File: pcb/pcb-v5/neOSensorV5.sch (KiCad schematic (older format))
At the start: 14 parts

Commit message: update pcb v5
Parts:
- removed J?: Conn_01x04, symbol Connector_Generic:Conn_01x04
- removed J?: Conn_01x08, symbol Connector_Generic:Conn_01x08
- added C?: 100nF, Resistor_SMD:R_0805_2012Metric_Pad1.20x1.40mm_HandSolder, symbol Device:C_Small
- added J?: Conn_01x05, Connector_PinHeader_2.54mm:PinHeader_1x05_P2.54mm_Vertical, symbol Connector_Generic:Conn_01x05
- added R? (x2): 4K7, symbol Device:R_Small
- added TP?: tp_tx2, TestPoint:TestPoint_Loop_D2.50mm_Drill1.0mm, symbol Connector:TestPoint
- added TP?: tp_rx2, TestPoint:TestPoint_Loop_D2.50mm_Drill1.0mm, symbol Connector:TestPoint
- C?: footprint (none) -> Capacitor_THT:CP_Radial_D6.3mm_P2.50mm
- H? (x2): value MountingHole_Pad -> 3.2mm for MH3 screw; footprint (none) -> MountingHole:MountingHole_3.2mm_M3_Pad
- J? (x2): footprint (none) -> Connector_PinHeader_2.54mm:PinHeader_1x04_P2.54mm_Vertical
- J? (x2): footprint (none) -> Connector_PinHeader_2.54mm:PinHeader_1x05_P2.54mm_Vertical
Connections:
- net labels added: +3V3, LED, PM_EN, RX2, TX2
- net labels removed: VIN
- wire segments 42 -> 68
- no-connect marks 0 -> 3
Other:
- note added: "Display"
- note added: "Notes about Particule Meters sensors\n- PM_EN is optionnally intended to enable/disable the\nparticule meter (not to have it always on)"
- note added: "Notes:\n- GPIO13 reserved for noise sensor\n- GPIO5 reserved for LED + clear sw\n- GPIO4 reserved for IR sensor (really?)\n- GPIO1 & GPIO3 are serial0 (prog.)\n- +3V3 on EN pin is optional"
- note added: "Power supply"
- note added: "TODO:\n- associate INT with an ESP32 pin"
- moved on the sheet: C?, H?, U?

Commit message: update
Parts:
- added D1: Red, LED_SMD:LED_0805_2012Metric_Pad1.15x1.40mm_HandSolder, symbol Device:LED_Small_ALT
- added Q1: 2N7002, Package_TO_SOT_SMD:SOT-23, symbol Transistor_FET:2N7002
- added R1: 68, Resistor_SMD:R_0805_2012Metric_Pad1.20x1.40mm_HandSolder, symbol Device:R_Small
- added R2, R9: 15k, Resistor_SMD:R_0805_2012Metric_Pad1.20x1.40mm_HandSolder, symbol Device:R_Small
- added R3, R7: 470, Resistor_SMD:R_0805_2012Metric_Pad1.20x1.40mm_HandSolder, symbol Device:R_Small
- added SW1: clear, neosensor_addon:G71Y_µsw_smd, symbol neosensor_addon:G71Y
- added U1: HC-SR01, neosensor_addon:PIR_HC-SR01, symbol neosensor_addon:HC-SR01
- R4, R8: renamed from R?; footprint (none) -> Resistor_SMD:R_0805_2012Metric_Pad1.20x1.40mm_HandSolder
- R5, R6: renamed from R?; value 220 -> 470; footprint (none) -> Resistor_SMD:R_0805_2012Metric_Pad1.20x1.40mm_HandSolder
- gave numbers to parts that had none: 14
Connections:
- net +3V3: now also SW1.2
- net +5V: now also D1.2 (A), U1.1 (V+)
- net GND: now also Q1.3 (D), R2.1, R9.1, SW1.3, U1.3 (GND)
- net INT: now also U3.10 (GPIO19)
- net LED: now also R3.1
- net at U3.5 (GPIO4): now also R7.2
- net ESP_RX2: no longer names the net of R6.2, U3.6 (GPIO16)
- net ESP_TX2: no longer names the net of R5.2, U3.7 (GPIO17)
- new net: Q1.1 (G), R2.2, R3.2, SW1.1
- new net: Q1.2 (S), R1.1
- new net: D1.1 (K), R1.2
- new net IR: R7.1, R9.2, U1.2 (OUT)
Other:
- note added: "HC-SR01 V+ accepts from 5 to 20v\nOUT pin is 3.3 TTL"
- note added: "LED and Clear_SW"
- note added: "Notes:\n- GPIO13 reserved for noise sensor\n- GPIO5 reserved for LED + clear sw\n- GPIO4 reserved for IR sensor\n- GPIO1 & GPIO3 are serial0 (prog.)\n- +3V3 on EN pin is optional"
- note added: "PIR sensor"
- note added: "TODO:\n"
- note removed: "Notes:\n- GPIO13 reserved for noise sensor\n- GPIO5 reserved for LED + clear sw\n- GPIO4 reserved for IR sensor (really?)\n- GPIO1 & GPIO3 are serial0 (prog.)\n- +3V3 on EN pin is optional"
- note removed: "TODO:\n- associate INT with an ESP32 pin"

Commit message: update neOSensor V5
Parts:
- added C3: 100nF, Resistor_SMD:R_0805_2012Metric_Pad1.20x1.40mm_HandSolder, symbol Device:C_Small
- added J6, J7: Conn_01x03, Connector_PinHeader_2.54mm:PinHeader_1x03_P2.54mm_Vertical, symbol Connector_Generic:Conn_01x03
- added R10, R12, R15, R18: 15k, Resistor_SMD:R_0805_2012Metric_Pad1.20x1.40mm_HandSolder, symbol Device:R_Small
- added R11, R13: 470, Resistor_SMD:R_0805_2012Metric_Pad1.20x1.40mm_HandSolder, symbol Device:R_Small
- added R14, R17: 2k, Resistor_SMD:R_0805_2012Metric_Pad1.20x1.40mm_HandSolder, symbol Device:R_Small
- added R16, R19: 33k, Resistor_SMD:R_0805_2012Metric_Pad1.20x1.40mm_HandSolder, symbol Device:R_Small
- added SW2: +, neosensor_addon:G71Y_µsw_smd, symbol neosensor_addon:G71Y
- added SW3: -, neosensor_addon:G71Y_µsw_smd, symbol neosensor_addon:G71Y
- added U5, U6: LM2902, Package_SO:SO-14_5.3x10.2mm_P1.27mm, symbol Amplifier_Operational:LM2902
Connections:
- net +3V3: now also C3.1, SW2.1, SW3.1, U5.4 (V+)
- net +5V: now also J6.1 (Pin_1), J7.1 (Pin_1)
- net GND: now also C3.2, J6.3 (Pin_3), J7.3 (Pin_3), R10.1, R12.1, R16.1, R19.1, SW2.3, SW3.3, U5.11 (V-)
- net SW3: now reaches U3.15 (GPIO23)
- net SW3: now also R13.1
- net ADC1_0: now reaches U3.17 (GPIO36)
- net ADC1_0: now also U5.1, U5.2 (-)
- net ADC1_3: now reaches U3.18 (GPIO39)
- net ADC1_3: now also U6.1, U6.2 (-)
- net SW2: now reaches U3.9 (GPIO18)
- net SW2: now also R11.1
- new net: R10.2, R11.2, SW2.2
- new net: R12.2, R13.2, SW3.2
- new net: R15.2, R16.2, U5.3 (+)
- new net: R14.2, R15.1
- new net: R18.2, R19.2, U6.3 (+)
- new net: R17.2, R18.1
- new net ANA_0: J6.2 (Pin_2), R14.1
- new net ANA_1: J7.2 (Pin_2), R17.1
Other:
- note added: "ANALOG inputs"
- note added: "LED and SWITCHES"
- note added: "Notes:\n- GPIO13 reserved for noise sensor\n- GPIO5 reserved for LED + clear sw\n- GPIO4 reserved for IR sensor\n- ADC2 pins cannot be used when WiFi in use\n- prefer ADC1 pins (GPIO32 --> 39)\n- GPIO1 & GPIO3 are serial0 (prog.)\n- +3V3 on EN pin is optional"
- note added: "Translate 5v analog input to 3v3\nV+ = 5v x 33k / 50k = 3.3v\nop. amp as follower"
- note removed: "LED and Clear_SW"
- note removed: "Notes:\n- GPIO13 reserved for noise sensor\n- GPIO5 reserved for LED + clear sw\n- GPIO4 reserved for IR sensor\n- GPIO1 & GPIO3 are serial0 (prog.)\n- +3V3 on EN pin is optional"
- moved on the sheet: D1, Q1, R1, R2, R3, SW1

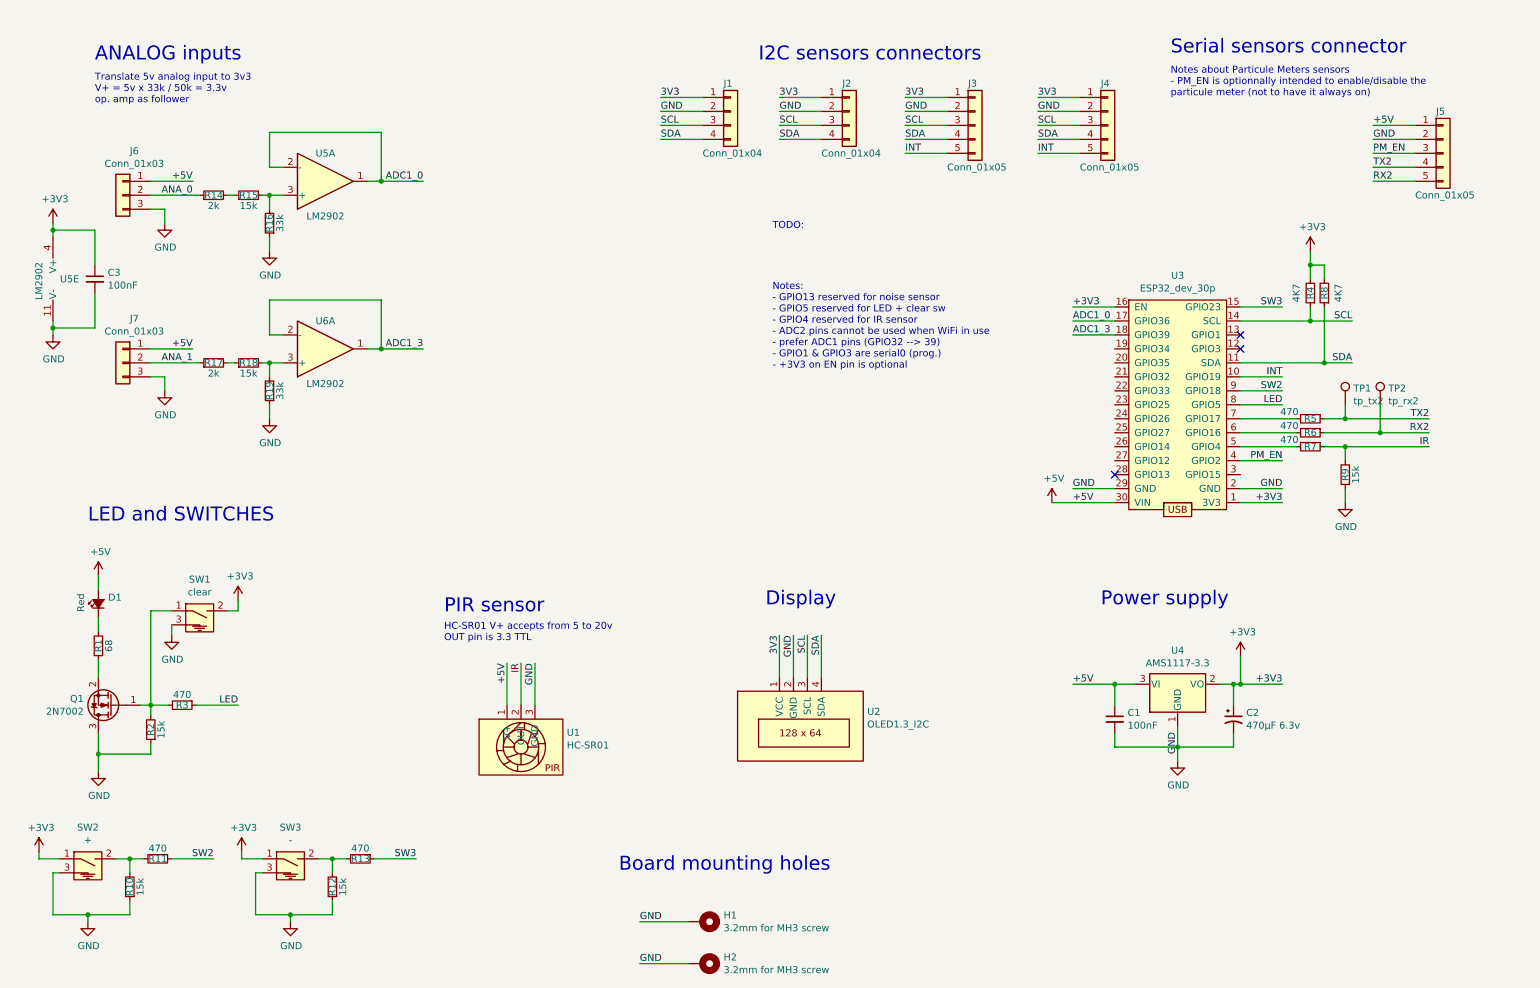
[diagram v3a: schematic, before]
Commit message: added analog inputs to pcb v5
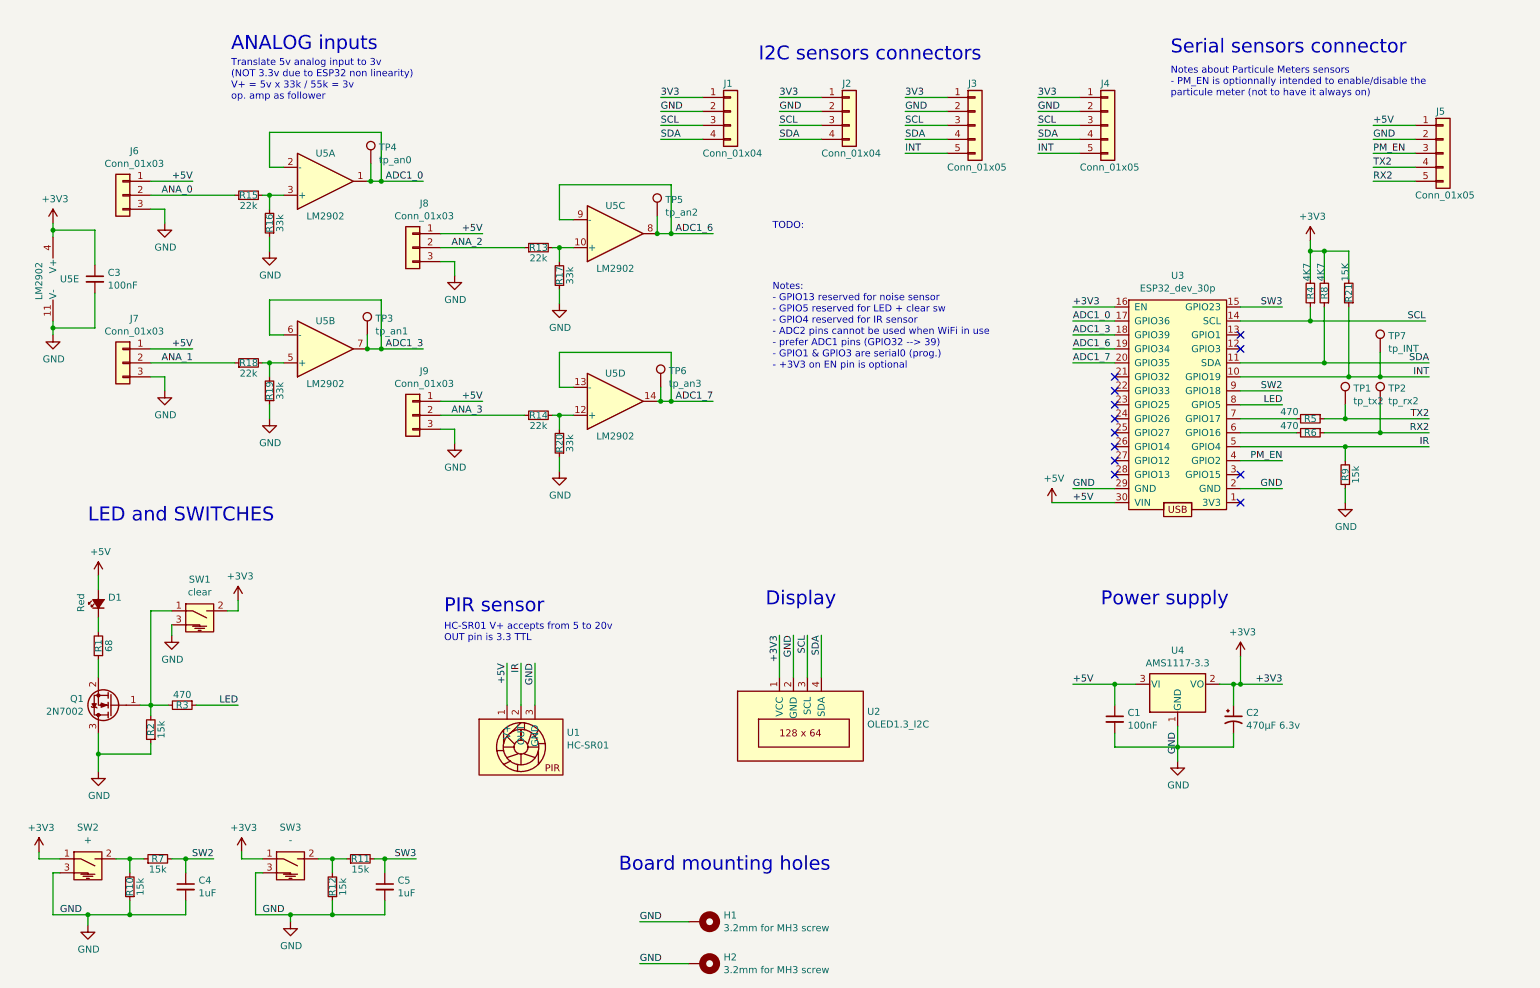
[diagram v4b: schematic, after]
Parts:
- removed U6: LM2902, Package_SO:SO-14_5.3x10.2mm_P1.27mm, symbol Amplifier_Operational:LM2902
- added C4, C5: 1uF, Resistor_SMD:R_0805_2012Metric_Pad1.20x1.40mm_HandSolder, symbol Device:C_Small
- added J8, J9: Conn_01x03, Connector_PinHeader_2.54mm:PinHeader_1x03_P2.54mm_Vertical, symbol Connector_Generic:Conn_01x03
- added R20: 33k, Resistor_SMD:R_0805_2012Metric_Pad1.20x1.40mm_HandSolder, symbol Device:R_Small
- added R21: 15K, Resistor_SMD:R_0805_2012Metric_Pad1.20x1.40mm_HandSolder, symbol Device:R_Small
- added TP3: tp_an1, TestPoint:TestPoint_Loop_D2.50mm_Drill1.0mm, symbol Connector:TestPoint
- added TP4: tp_an0, TestPoint:TestPoint_Loop_D2.50mm_Drill1.0mm, symbol Connector:TestPoint
- added TP5: tp_an2, TestPoint:TestPoint_Loop_D2.50mm_Drill1.0mm, symbol Connector:TestPoint
- added TP6: tp_an3, TestPoint:TestPoint_Loop_D2.50mm_Drill1.0mm, symbol Connector:TestPoint
- added TP7: tp_INT, TestPoint:TestPoint_Loop_D2.50mm_Drill1.0mm, symbol Connector:TestPoint
- added unit 2 of U5
- added unit 3 of U5
- added unit 4 of U5
- R11, R7: value 470 -> 15k
- R13: value 470 -> 22k
- R14: value 2k -> 22k
- R15, R18: value 15k -> 22k
- R17: value 2k -> 33k
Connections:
- net +3V3: now also U2.1 (VCC), R21.2; no longer U3.1 (3V3)
- net +5V: now also J8.1 (Pin_1), J9.1 (Pin_1)
- net 3V3: no longer U2.1 (VCC)
- net ADC1_0: now also TP4.1
- net ADC1_3: now also TP3.1, U5.6 (-), U5.7
- net ANA_0: now also R15.1; no longer R14.1
- net ANA_1: now also R18.1; no longer R17.1
- net GND: now also R17.1, C4.2, C5.2, J8.3 (Pin_3), J9.3 (Pin_3), R20.1
- net INT: now also R21.1, TP7.1
- net IR: now also U3.5 (GPIO4); no longer R7.1
- net SW2: now also R7.2, C4.1; no longer R11.1
- net SW3: now also R11.2, C5.1; no longer R13.1
- net ADC1_6: now reaches U3.19 (GPIO34)
- net ADC1_6: now also TP5.1, U5.8, U5.9 (-)
- net ADC1_7: now reaches U3.20 (GPIO35)
- net ADC1_7: now also TP6.1, U5.13 (-), U5.14
- net at R10.2, SW2.2: now also R7.1; no longer R11.2
- net at R12.2, SW3.2: now also R11.1; no longer R13.2
- net at R14.2: now also R20.2, U5.12 (+); no longer R15.1
- net at R18.2, R19.2: now also U5.5 (+)
- net at R17.2: now also R13.2, U5.10 (+); no longer R18.1
- new net ANA_2: J8.2 (Pin_2), R13.1
- new net ANA_3: J9.2 (Pin_2), R14.1
- no-connect marks 3 -> 12
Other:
- note added: "Translate 5v analog input to 3v\n(NOT 3.3v due to ESP32 non linearity)\nV+ = 5v x 33k / 55k = 3v\nop. amp as follower"
- note removed: "Translate 5v analog input to 3v3\nV+ = 5v x 33k / 50k = 3.3v\nop. amp as follower"

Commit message: update
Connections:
- net 3V3 is gone; now on net +3V3: J1.1 (Pin_1), J2.1 (Pin_1), J3.1 (Pin_1), J4.1 (Pin_1)
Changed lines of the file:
@@
 Text Notes 4950 6700 0    100  ~ 0
 Board mounting holes
-$Comp
-L power:GND #PWR06
-U 1 1 601C1C3A
-P 8950 5900
-F 0 "#PWR06" H 8950 5650 50  0001 C CNN
-F 1 "GND" H 8955 5727 50  0000 C CNN
-F 2 "" H 8950 5900 50  0001 C CNN
-F 3 "" H 8950 5900 50  0001 C CNN
-	1    8950 5900
-	1    0    0    -1
-$EndComp
 Wire Wire Line
 	8950 5900 8950 5800
@@
 	5550 1150 5250 1150
 Text Label 5250 1150 0    50   ~ 0
-3V3
++3V3
 Wire Wire Line
 	5250 1250 5550 1250
@@
 	6400 1150 6100 1150
 Text Label 6100 1150 0    50   ~ 0
-3V3
++3V3
 Wire Wire Line
 	6100 1250 6400 1250
@@
 	7300 1150 7000 1150
 Text Label 7000 1150 0    50   ~ 0
-3V3
++3V3
 Wire Wire Line
 	7000 1250 7300 1250
@@
 	8250 1150 7950 1150
 Text Label 7950 1150 0    50   ~ 0
-3V3
++3V3
 Wire Wire Line
 	7950 1250 8250 1250
@@
 L power:GND #PWR03
 U 1 1 60224902
-P 1750 5000
-F 0 "#PWR03" H 1750 4750 50  0001 C CNN
-F 1 "GND" H 1755 4827 50  0000 C CNN
-F 2 "" H 1750 5000 50  0001 C CNN
-F 3 "" H 1750 5000 50  0001 C CNN
-	1    1750 5000
-	1    0    0    -1
-$EndComp
-Wire Wire Line
-	1750 4925 1750 5000
+P 1750 5025
+F 0 "#PWR03" H 1750 4775 50  0001 C CNN
+F 1 "GND" H 1755 4852 50  0000 C CNN
+F 2 "" H 1750 5025 50  0001 C CNN
+F 3 "" H 1750 5025 50  0001 C CNN
+	1    1750 5025
+	1    0    0    -1
+$EndComp
+Wire Wire Line
+	1750 4925 1750 5025
 Wire Wire Line
 	1750 4825 1600 4825
@@
 Wire Wire Line
 	4525 3425 4525 3525
-$Comp
-L power:GND #PWR019
-U 1 1 603101AF
-P 4525 3825
-F 0 "#PWR019" H 4525 3575 50  0001 C CNN
-F 1 "GND" H 4530 3652 50  0000 C CNN
-F 2 "" H 4525 3825 50  0001 C CNN
-F 3 "" H 4525 3825 50  0001 C CNN
-	1    4525 3825
-	1    0    0    -1
-$EndComp
 Wire Wire Line
 	4525 3725 4525 3825
@@
 Text Label 3975 3325 2    50   ~ 0
 +5V
-$Comp
-L power:GND #PWR017
-U 1 1 603101D2
-P 3775 3625
-F 0 "#PWR017" H 3775 3375 50  0001 C CNN
-F 1 "GND" H 3780 3452 50  0000 C CNN
-F 2 "" H 3775 3625 50  0001 C CNN
-F 3 "" H 3775 3625 50  0001 C CNN
-	1    3775 3625
-	1    0    0    -1
-$EndComp
 Wire Wire Line
 	3675 3525 3775 3525
@@
 Text Label 2400 7000 0    50   ~ 0
 GND
+$Comp
+L power:GND #PWR0105
+U 1 1 60232079
+P 4525 3825
+F 0 "#PWR0105" H 4525 3575 50  0001 C CNN
+F 1 "GND" H 4530 3652 50  0000 C CNN
+F 2 "" H 4525 3825 50  0001 C CNN
+F 3 "" H 4525 3825 50  0001 C CNN
+	1    4525 3825
+	1    0    0    -1
+$EndComp
+$Comp
+L power:GND #PWR0106
+U 1 1 60232CA5
+P 8950 5900
+F 0 "#PWR0106" H 8950 5650 50  0001 C CNN
+F 1 "GND" H 8955 5727 50  0000 C CNN
+F 2 "" H 8950 5900 50  0001 C CNN
+F 3 "" H 8950 5900 50  0001 C CNN
+	1    8950 5900
+	1    0    0    -1
+$EndComp
+$Comp
+L power:GND #PWR0107
+U 1 1 602338CC
+P 3775 3625
+F 0 "#PWR0107" H 3775 3375 50  0001 C CNN
+F 1 "GND" H 3780 3452 50  0000 C CNN
+F 2 "" H 3775 3625 50  0001 C CNN
+F 3 "" H 3775 3625 50  0001 C CNN
+	1    3775 3625
+	1    0    0    -1
+$EndComp
 $EndSCHEMATC

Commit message: update pcb V5
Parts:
- removed J6, J7, J8, J9: Conn_01x03, Connector_PinHeader_2.54mm:PinHeader_1x03_P2.54mm_Vertical, symbol Connector_Generic:Conn_01x03
- added J6: Conn_01x06, Connector_PinHeader_2.54mm:PinHeader_1x06_P2.54mm_Vertical, symbol Connector_Generic:Conn_01x06
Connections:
- net +5V: now also J6.1 (Pin_1)
- net ANA_0: now also J6.3 (Pin_3)
- net ANA_1: now also J6.4 (Pin_4)
- net ANA_2: now also J6.5 (Pin_5)
- net ANA_3: now also J6.6 (Pin_6)
- net GND: now also J6.2 (Pin_2)
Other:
- moved on the sheet: R13, R14, R15, R16, R17, R18, R19, R20, TP3, TP4, TP5, TP6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
